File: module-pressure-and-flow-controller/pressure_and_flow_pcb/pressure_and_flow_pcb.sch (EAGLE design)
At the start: 38 parts, among them IC2 DSPIC33CK256MP502-I_SS, IC3 AD5624R, IC4 ADS1115, IC5 PCA9544APW,112, IC6 25AA040ST, X1 53047-04, X2 53047-04, X3 53047-04, X4 53047-04, X5 53047-04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

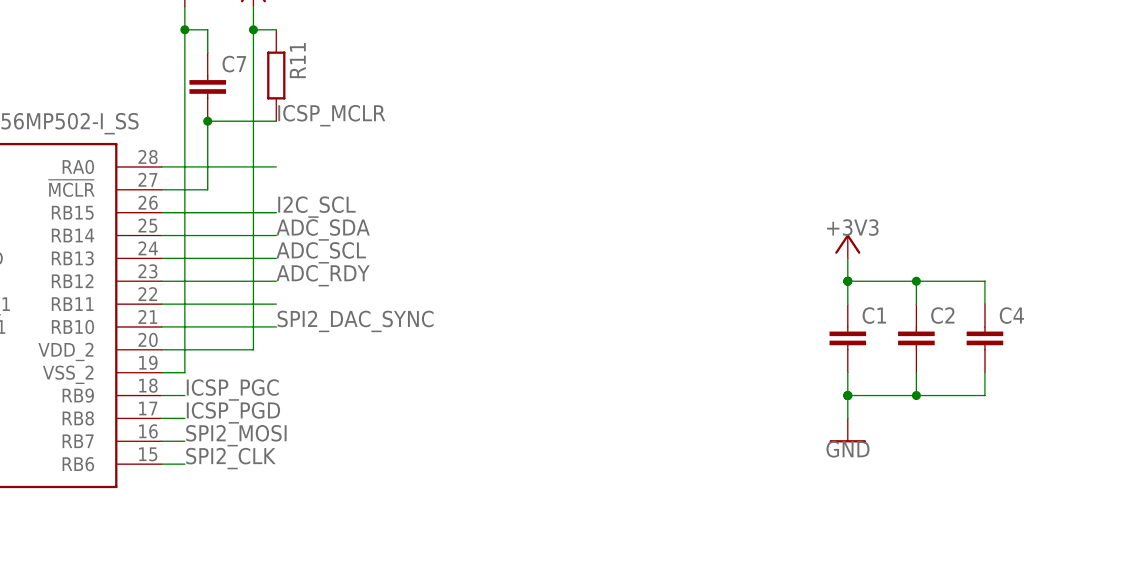
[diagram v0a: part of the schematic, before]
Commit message: Added bulk cap and changed caps to Kemet, which have smaller keepout.
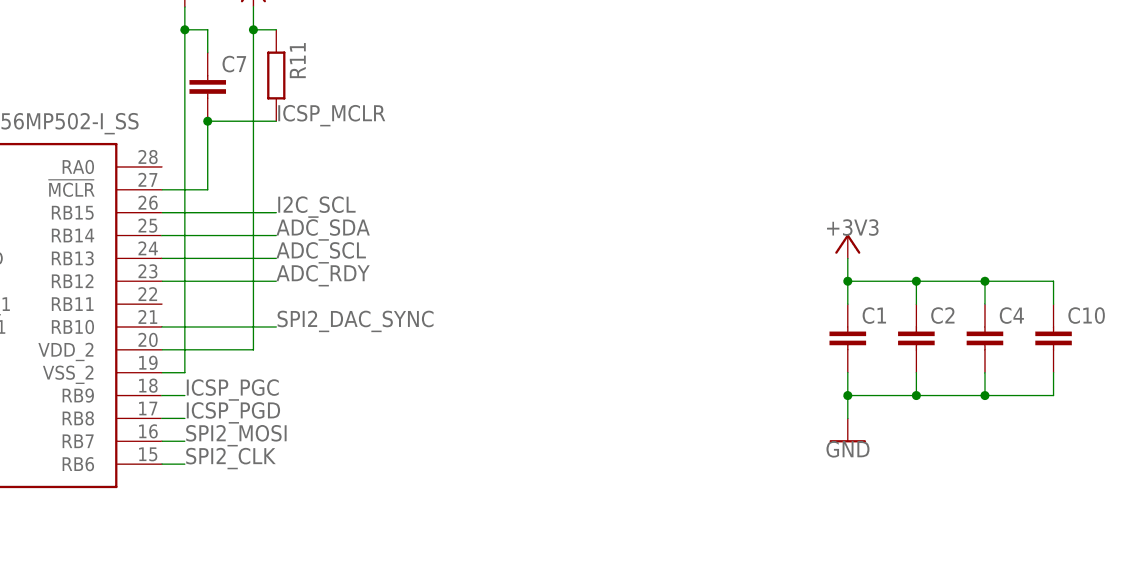
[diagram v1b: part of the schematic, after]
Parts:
- added C10: (no value), rcl:C-EUC0603K
- C1, C2, C3, C4, C5, C6, C7, C8, C9: device rcl:C-EUC0603 -> rcl:C-EUC0603K
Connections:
- removed net N$33: IC2.RB11
- removed net N$37: IC2.RA0
- net +3V3: now also C10.1
- net GND: now also C10.2

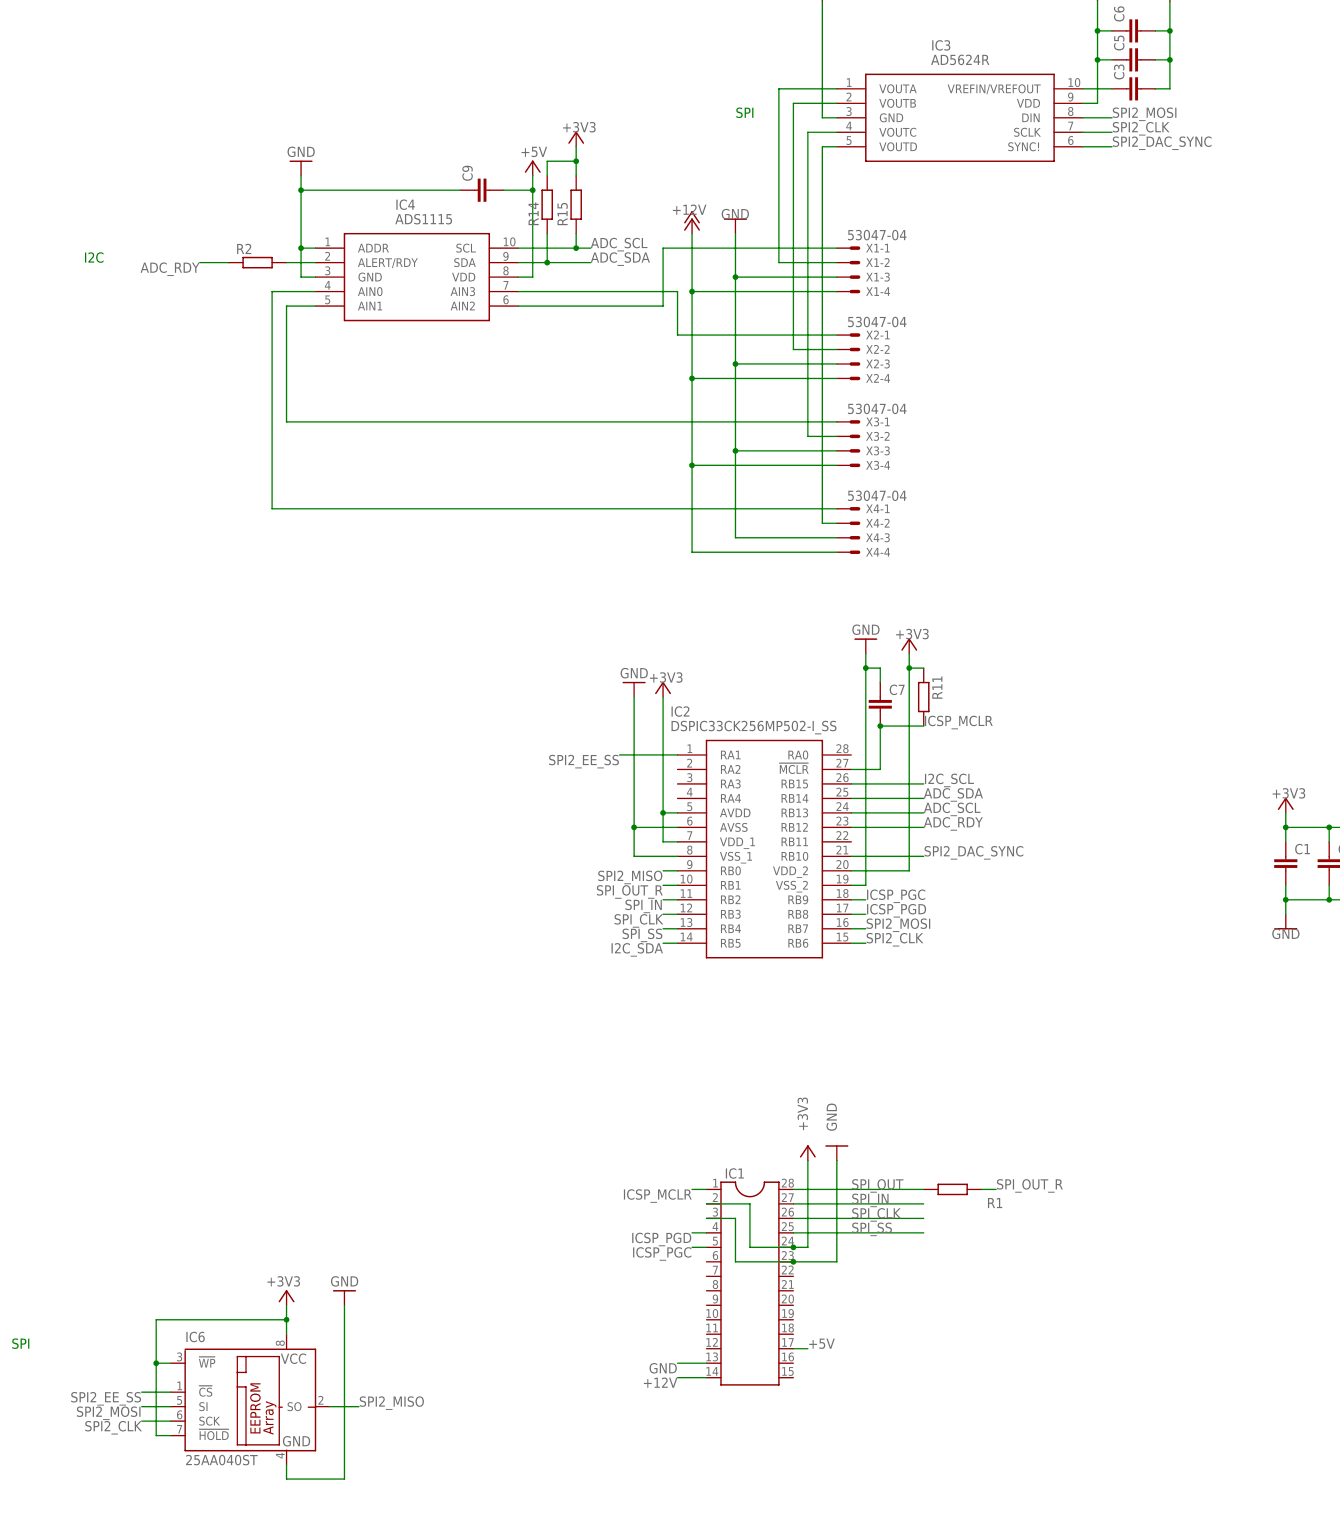
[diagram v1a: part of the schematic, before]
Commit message: PCB modifications to get I2C on correct pins and use extra SPI for EEPROM.  Code updated to match new pinout.
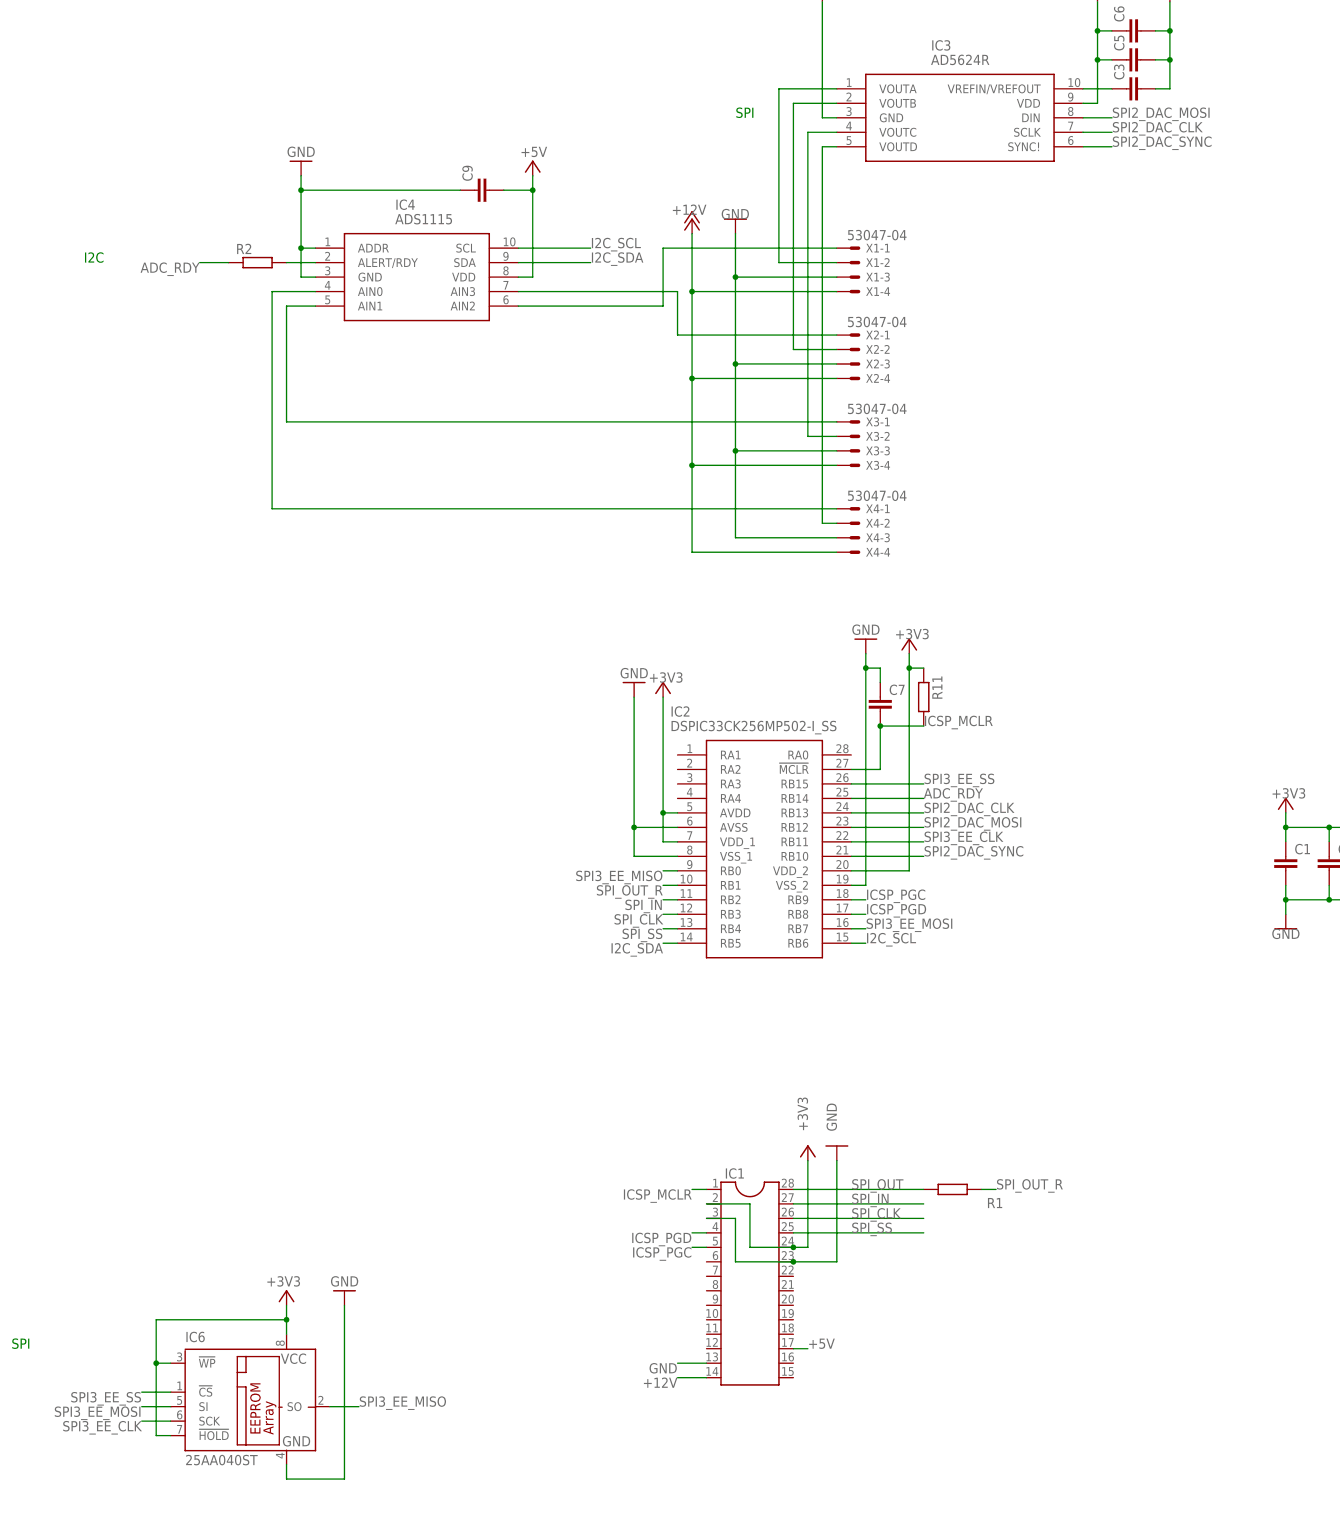
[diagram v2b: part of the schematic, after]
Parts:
- removed R14, R15: (no value), rcl:R-EU_R0603
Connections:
- net SPI2_MISO renamed SPI3_EE_MISO
- removed net ADC_SCL: IC2.RB13, IC4.SCL, R15.1
- removed net ADC_SDA: IC2.RB14, IC4.SDA, R14.1
- removed net SPI2_CLK: IC2.RB6, IC3.SCLK, IC6.SCK
- removed net SPI2_EE_SS: IC2.RA1, IC6.!CS
- removed net SPI2_MOSI: IC2.RB7, IC3.DIN, IC6.SI
- new net SPI2_DAC_CLK: IC2.RB13, IC3.SCLK
- new net SPI2_DAC_MOSI: IC2.RB12, IC3.DIN
- new net SPI3_EE_CLK: IC2.RB11, IC6.SCK
- new net SPI3_EE_MOSI: IC2.RB7, IC6.SI
- new net SPI3_EE_SS: IC2.RB15, IC6.!CS
- net +3V3: no longer R14.2, R15.2
- net ADC_RDY: now also IC2.RB14; no longer IC2.RB12
- net I2C_SCL: now also IC2.RB6, IC4.SCL; no longer IC2.RB15
- net I2C_SDA: now also IC4.SDA

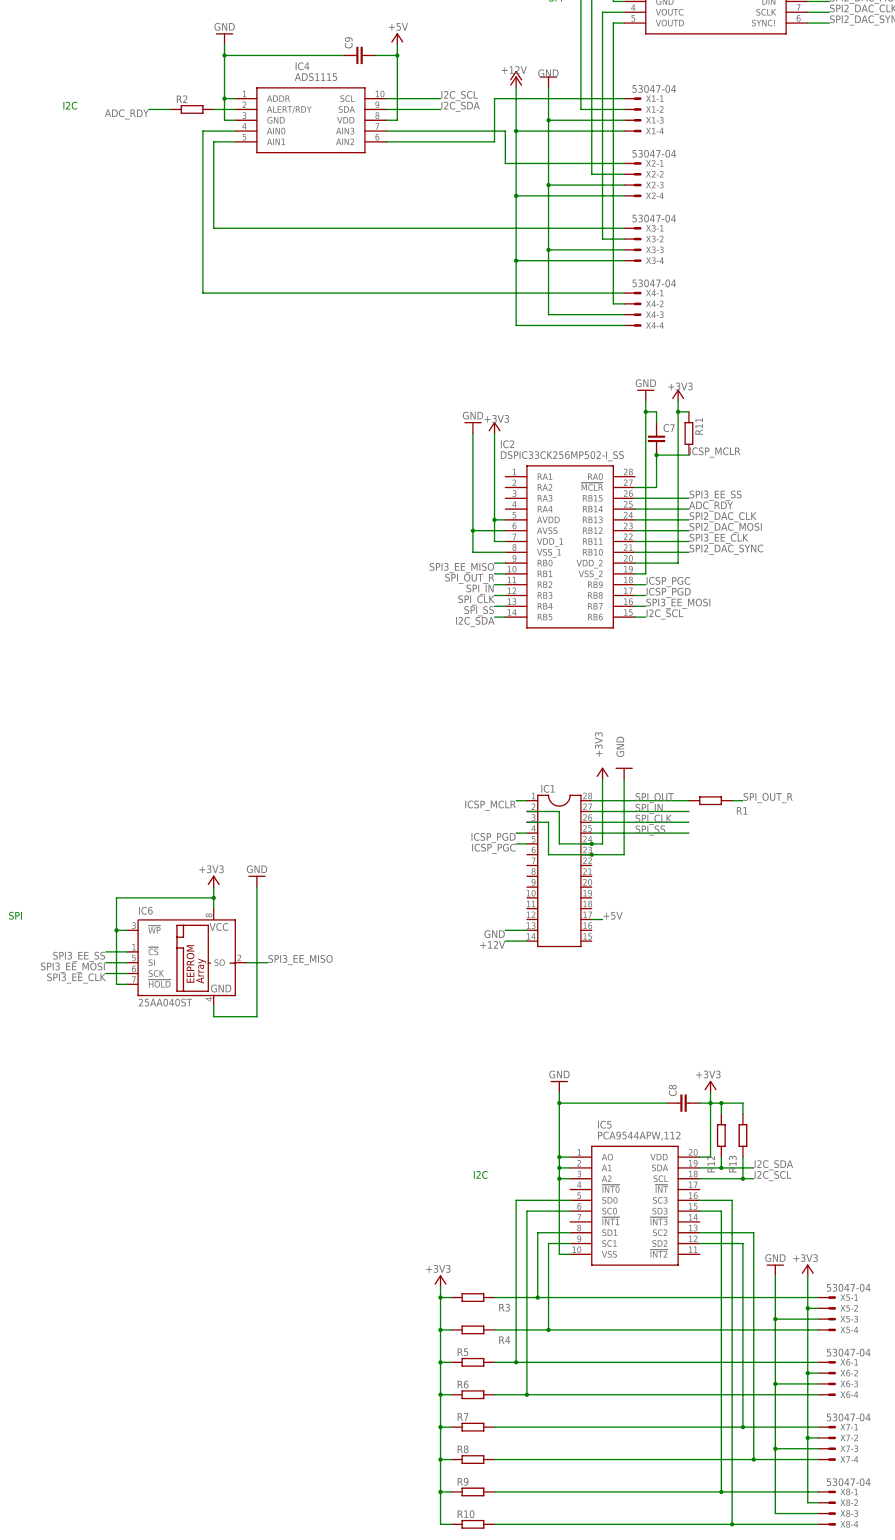
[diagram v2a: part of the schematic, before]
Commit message: Pull up I2C MUX int pins to VCC.
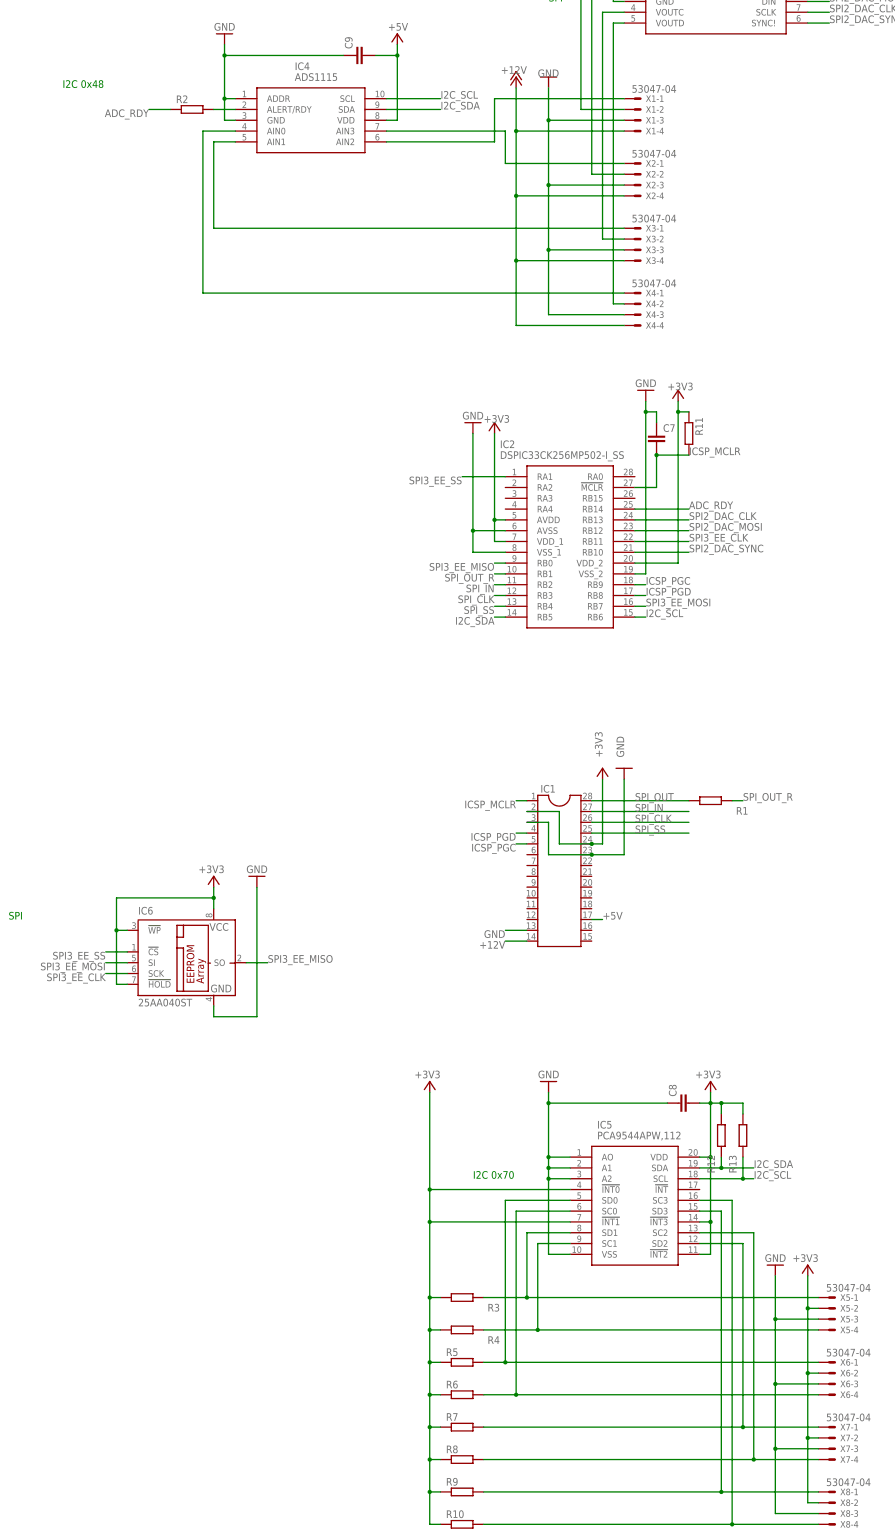
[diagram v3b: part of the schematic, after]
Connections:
- net +3V3: now also IC5.!INT0, IC5.!INT1, IC5.!INT2, IC5.!INT3
- net SPI3_EE_SS: now also IC2.RA1; no longer IC2.RB15
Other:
- note added: "I2C 0x48"
- note added: "I2C 0x70"
- note removed: "I2C"
- moved on the sheet: R10, R3, R4, R5, R6, R7, R8, R9
